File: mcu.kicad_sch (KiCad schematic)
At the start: 22 parts, among them J1 FTSH-105-01-F-DV-P-TR, U1 nRF52840, U5 MX25R6435FZAIL0, U6 AP22814AW5, Y1 32MHz, Y2 32.768kHz

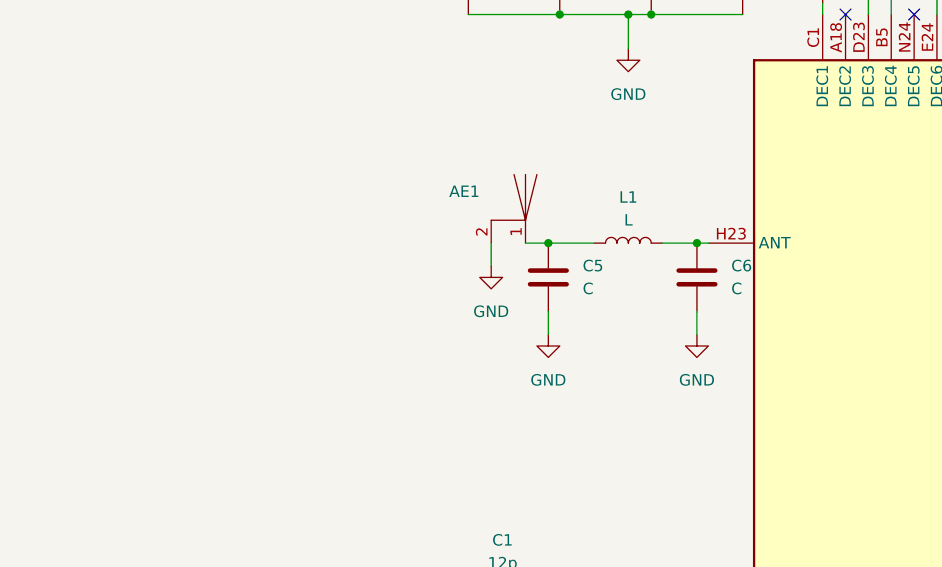
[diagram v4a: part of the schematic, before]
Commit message: Added impedance match, gitignore
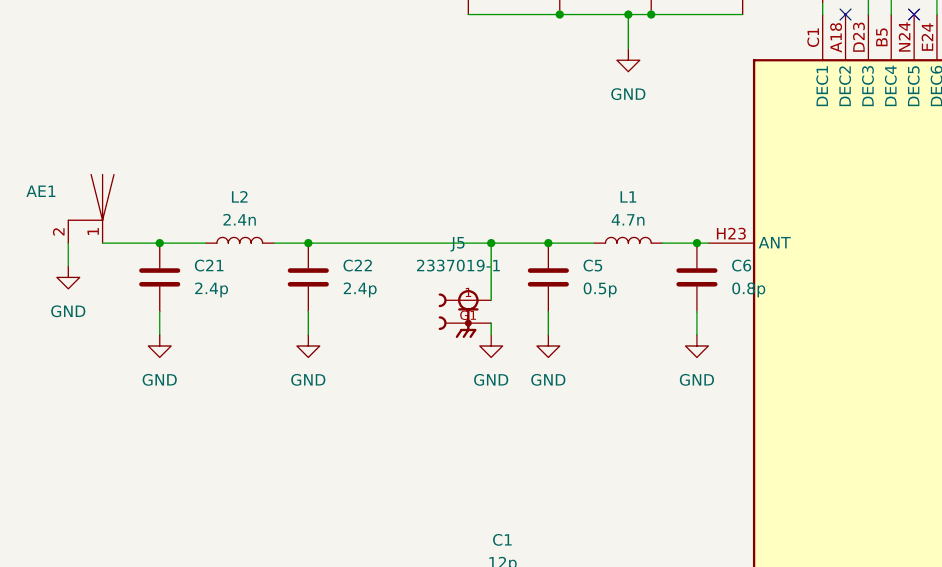
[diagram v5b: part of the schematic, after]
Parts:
- added C21, C22: 2.4p, symbol Device:C
- added J5: 2337019-1, Personal:TE_2337019-1, symbol generic:2337019-1
- added L2: 2.4n, symbol Device:L
- C5: value C -> 0.5p
- C6: value C -> 0.8p
- L1: value L -> 4.7n
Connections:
- net GND: now also C21.2, C22.2, J5.G1
- net at C5.1, L1.1: now also C22.1, J5.1, L2.2; no longer AE1.1
- new net: AE1.1, C21.1, L2.1
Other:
- moved on the sheet: AE1

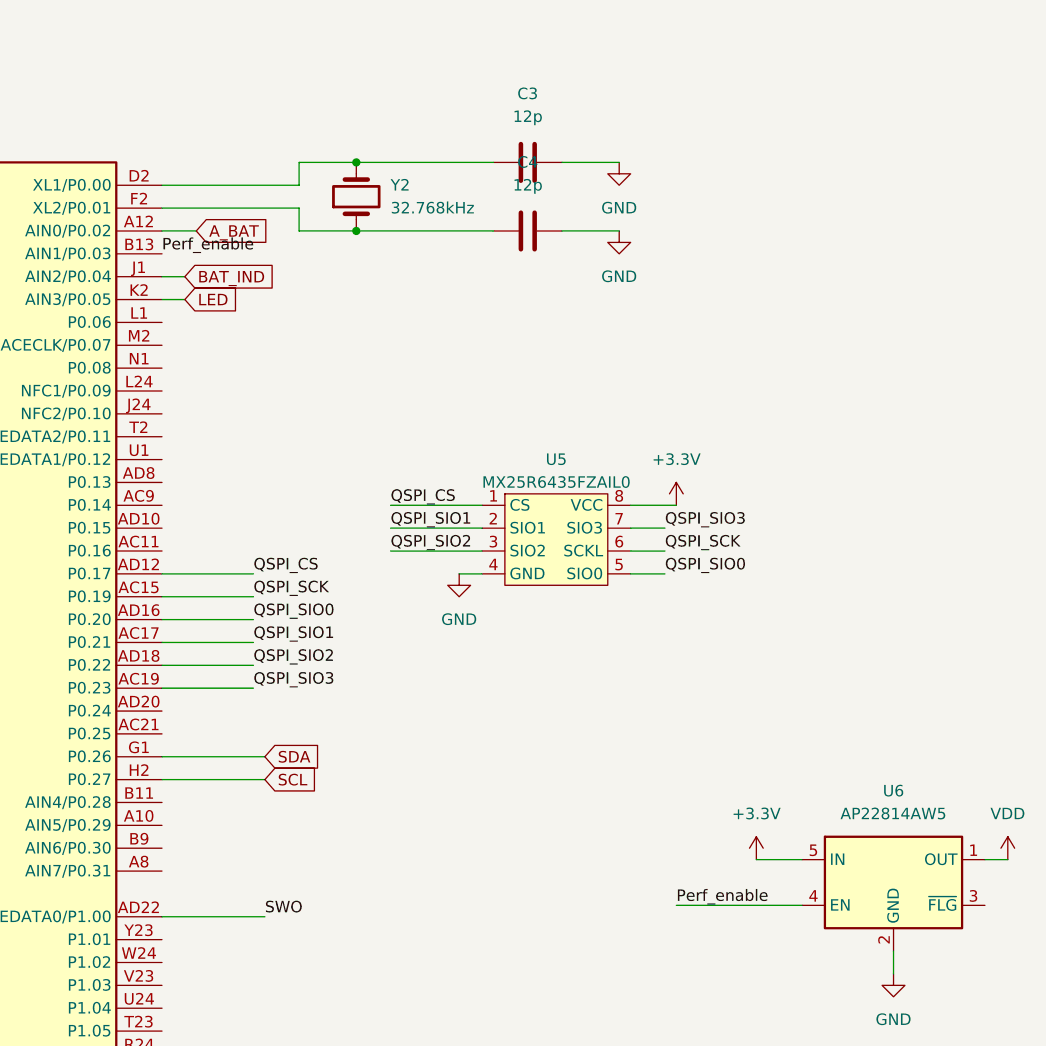
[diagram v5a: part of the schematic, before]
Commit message: Added microphone, fuse
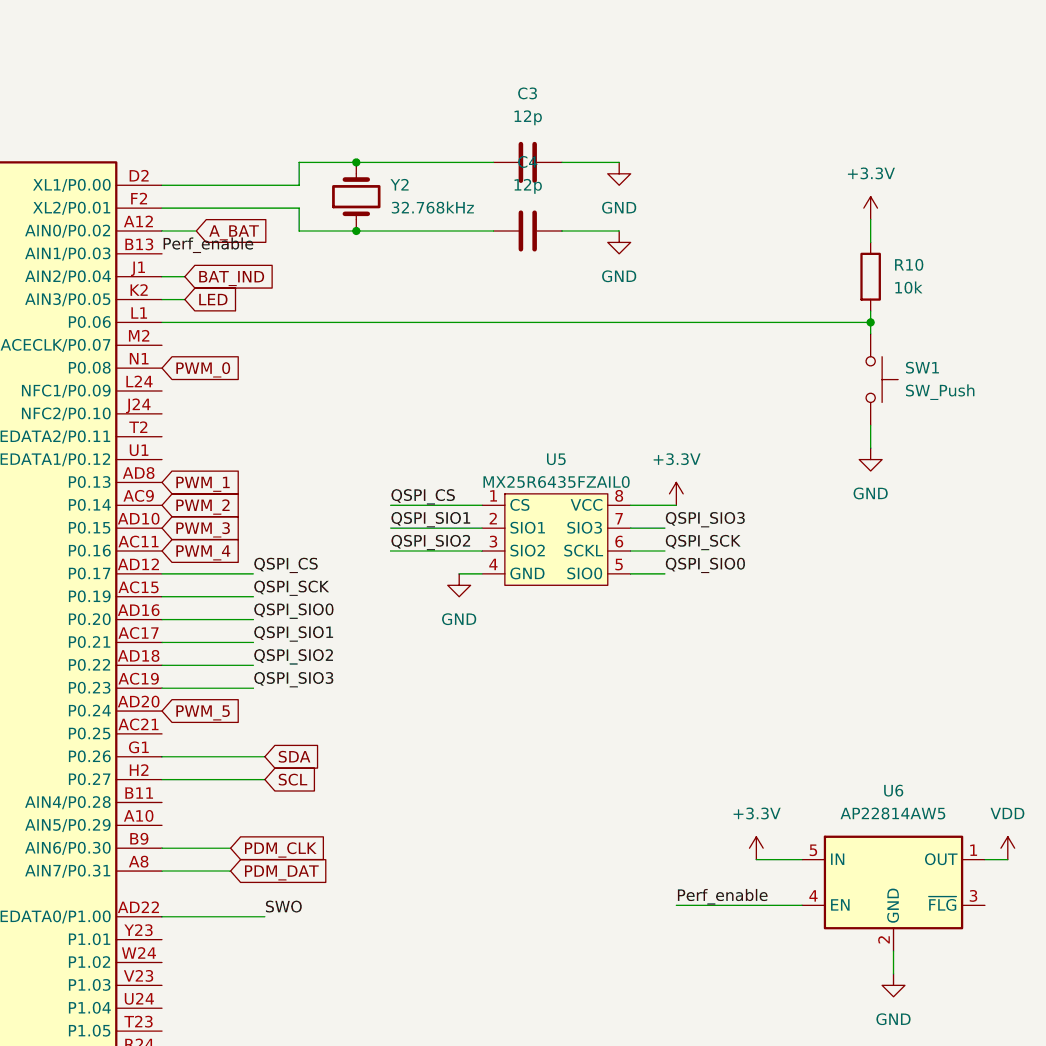
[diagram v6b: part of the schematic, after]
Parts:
- added R10: 10k, symbol Device:R
- added SW1: SW_Push, Button_Switch_THT:SW_PUSH_6mm, symbol Switch:SW_Push
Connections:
- net +3.3V: now also R10.1
- net GND: now also SW1.2
- net PDM_DAT: now reaches U1.A8 (AIN7/P0.31)
- net PWM_4: now reaches U1.AC11 (P0.16)
- net PWM_2: now reaches U1.AC9 (P0.14)
- net PWM_3: now reaches U1.AD10 (P0.15)
- net PWM_5: now reaches U1.AD20 (P0.24)
- net PWM_1: now reaches U1.AD8 (P0.13)
- net PDM_CLK: now reaches U1.B9 (AIN6/P0.30)
- net at U1.L1 (P0.06): now also R10.2, SW1.1
- net PWM_0: now reaches U1.N1 (P0.08)

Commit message: finished schematic
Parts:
- C1, C2, C3, C4: footprint (none) -> Capacitor_SMD:C_0603_1608Metric; LCSC PN (none) -> C107034
- C11, C17: footprint (none) -> Capacitor_SMD:C_0603_1608Metric; LCSC PN (none) -> C15849
- C12, C13, C16: value 100n -> .1u; footprint (none) -> Capacitor_SMD:C_0603_1608Metric; LCSC PN (none) -> C14663
- C14, C15: footprint (none) -> Capacitor_SMD:C_0603_1608Metric; LCSC PN (none) -> C19666
- C18: footprint (none) -> Capacitor_SMD:C_0603_1608Metric; LCSC PN (none) -> C14665
- C21, C22: footprint (none) -> Capacitor_SMD:C_0603_1608Metric; LCSC PN (none) -> C710896
- C5: footprint (none) -> Capacitor_SMD:C_0603_1608Metric; LCSC PN (none) -> C162254
- C6: footprint (none) -> Capacitor_SMD:C_0603_1608Metric; LCSC PN (none) -> C907996
- L1: footprint (none) -> Inductor_SMD:L_0603_1608Metric; LCSC PN (none) -> C98078
- L2: footprint (none) -> Inductor_SMD:L_0603_1608Metric; LCSC PN (none) -> C2042508
- R10: footprint (none) -> Resistor_SMD:R_0603_1608Metric; LCSC PN (none) -> C98220
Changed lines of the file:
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@@
 			)
 		)
-		(property "Footprint" ""
+		(property "Footprint" "Capacitor_SMD:C_0603_1608Metric"
 			(at 111.4552 20.32 0)
 			(effects
@@
 			)
 		)
+		(property "LCSC PN" "C14665"
+			(at 110.49 16.51 0)
+			(effects
+				(font
+					(size 1.27 1.27)
+				)
+				(hide yes)
+			)
+		)
 		(pin "2"
 		)
@@
 			)
 		)
-		(property "Footprint" ""
+		(property "Footprint" "Capacitor_SMD:C_0603_1608Metric"
 			(at 113.9952 25.4 0)
 			(effects
@@
 			)
 		)
+		(property "LCSC PN" "C15849"
+			(at 113.03 21.59 0)
+			(effects
+				(font
+					(size 1.27 1.27)
+				)
+				(hide yes)
+			)
+		)
 		(pin "2"
 		)
@@
 			)
 		)
-		(property "Value" "100n"
+		(property "Value" ".1u"
 			(at 100.33 25.3999 0)
 			(effects
@@
 			)
 		)
-		(property "Footprint" ""
+		(property "Footprint" "Capacitor_SMD:C_0603_1608Metric"
 			(at 97.4852 27.94 0)
 			(effects
@@
 			)
 		)
+		(property "LCSC PN" "C14663"
+			(at 96.52 24.13 0)
+			(effects
+				(font
+					(size 1.27 1.27)
+				)
+				(hide yes)
+			)
+		)
 		(pin "2"
 		)
@@
 			)
 		)
-		(property "Footprint" ""
+		(property "Footprint" "Capacitor_SMD:C_0603_1608Metric"
 			(at 72.39 103.1748 0)
 			(effects
@@
 			)
 		)
+		(property "LCSC PN" "C107034"
+			(at 68.58 104.14 90)
+			(effects
+				(font
+					(size 1.27 1.27)
+				)
+				(hide yes)
+			)
+		)
 		(pin "2"
 		)
@@
 			)
 		)
-		(property "Footprint" ""
+		(property "Footprint" "Capacitor_SMD:C_0603_1608Metric"
 			(at 75.8952 60.96 0)
 			(effects
@@
 			)
 		)
+		(property "LCSC PN" "C162254"
+			(at 74.93 57.15 0)
+			(effects
+				(font
+					(size 1.27 1.27)
+				)
+				(hide yes)
+			)
+		)
 		(pin "2"
 		)
@@
 			)
 		)
-		(property "Footprint" ""
+		(property "Footprint" "Inductor_SMD:L_0603_1608Metric"
 			(at 40.64 53.34 0)
 			(effects
@@
 			)
 		)
+		(property "LCSC PN" "C2042508"
+			(at 40.64 53.34 90)
+			(effects
+				(font
+					(size 1.27 1.27)
+				)
+				(hide yes)
+			)
+		)
 		(pin "2"
 		)
@@
 			)
 		)
-		(property "Value" "100n"
+		(property "Value" ".1u"
 			(at 109.22 24.1299 0)
 			(effects
@@
 			)
 		)
-		(property "Footprint" ""
+		(property "Footprint" "Capacitor_SMD:C_0603_1608Metric"
 			(at 106.3752 26.67 0)
 			(effects
@@
 			)
 		)
+		(property "LCSC PN" "C14663"
+			(at 105.41 22.86 0)
+			(effects
+				(font
+					(size 1.27 1.27)
+				)
+				(hide yes)
+			)
+		)
 		(pin "2"
 		)
@@
 			)
 		)
-		(property "Footprint" ""
+		(property "Footprint" "Capacitor_SMD:C_0603_1608Metric"
 			(at 32.7152 60.96 0)
 			(effects
@@
 			)
 		)
+		(property "LCSC PN" "C710896"
+			(at 31.75 57.15 0)
+			(effects
+				(font
+					(size 1.27 1.27)
+				)
+				(hide yes)
+			)
+		)
 		(pin "2"
 		)
@@
 			)
 		)
-		(property "Footprint" ""
+		(property "Footprint" "Capacitor_SMD:C_0603_1608Metric"
 			(at 77.1652 27.94 0)
 			(effects
@@
 			)
 		)
+		(property "LCSC PN" "C15849"
+			(at 76.2 24.13 0)
+			(effects
+				(font
+					(size 1.27 1.27)
+				)
+				(hide yes)
+			)
+		)
 		(pin "2"
 		)
@@
 			)
 		)
-		(property "Footprint" ""
+		(property "Footprint" "Inductor_SMD:L_0603_1608Metric"
 			(at 83.82 53.34 0)
 			(effects
@@
 			)
 		)
+		(property "LCSC PN" "C98078"
+			(at 83.82 53.34 90)
+			(effects
+				(font
+					(size 1.27 1.27)
+				)
+				(hide yes)
+			)
+		)
 		(pin "2"
 		)
@@
 			)
 		)
-		(property "Footprint" ""
+		(property "Footprint" "Capacitor_SMD:C_0603_1608Metric"
 			(at 119.6848 20.32 0)
 			(effects
@@
 			)
 		)
+		(property "LCSC PN" "C19666"
+			(at 120.65 24.13 0)
+			(effects
+				(font
+					(size 1.27 1.27)
+				)
+				(hide yes)
+			)
+		)
 		(pin "2"
 		)
@@
 			)
 		)
-		(property "Footprint" ""
+		(property "Footprint" "Capacitor_SMD:C_0603_1608Metric"
 			(at 203.2 32.0548 0)
 			(effects
@@
 			)
 		)
+		(property "LCSC PN" "C107034"
+			(at 199.39 33.02 90)
+			(effects
+				(font
+					(size 1.27 1.27)
+				)
+				(hide yes)
+			)
+		)
 		(pin "2"
 		)
@@
 			)
 		)
-		(property "Footprint" ""
+		(property "Footprint" "Capacitor_SMD:C_0603_1608Metric"
 			(at 92.4052 60.96 0)
 			(effects
@@
 			)
 		)
+		(property "LCSC PN" "C907996"
+			(at 91.44 57.15 0)
+			(effects
+				(font
+					(size 1.27 1.27)
+				)
+				(hide yes)
+			)
+		)
 		(pin "1"
 		)
@@
 			)
 		)
-		(property "Footprint" ""
+		(property "Footprint" "Resistor_SMD:R_0603_1608Metric"
 			(at 235.712 45.72 90)
 			(effects
@@
 			)
 		)
+		(property "LCSC PN" "C98220"
+			(at 237.49 45.72 0)
+			(effects
+				(font
+					(size 1.27 1.27)
+				)
+				(hide yes)
+			)
+		)
 		(pin "1"
 		)
@@
 			)
 		)
-		(property "Footprint" ""
+		(property "Footprint" "Capacitor_SMD:C_0603_1608Metric"
 			(at 203.2 39.6748 0)
 			(effects
@@
 			)
 		)
+		(property "LCSC PN" "C107034"
+			(at 199.39 40.64 90)
+			(effects
+				(font
+					(size 1.27 1.27)
+				)
+				(hide yes)
+			)
+		)
 		(pin "1"
 		)
@@
 			)
 		)
-		(property "Footprint" ""
+		(property "Footprint" "Capacitor_SMD:C_0603_1608Metric"
 			(at 67.0052 27.94 0)
 			(effects
@@
 			)
 		)
+		(property "LCSC PN" "C19666"
+			(at 66.04 24.13 0)
+			(effects
+				(font
+					(size 1.27 1.27)
+				)
+				(hide yes)
+			)
+		)
 		(pin "2"
 		)
@@
 			)
 		)
-		(property "Footprint" ""
+		(property "Footprint" "Capacitor_SMD:C_0603_1608Metric"
 			(at 73.66 93.0148 0)
 			(effects
@@
 			)
 		)
+		(property "LCSC PN" "C107034"
+			(at 69.85 93.98 90)
+			(effects
+				(font
+					(size 1.27 1.27)
+				)
+				(hide yes)
+			)
+		)
 		(pin "1"
 		)
@@
 			)
 		)
-		(property "Footprint" ""
+		(property "Footprint" "Capacitor_SMD:C_0603_1608Metric"
 			(at 49.2252 60.96 0)
 			(effects
@@
 			)
 		)
+		(property "LCSC PN" "C710896"
+			(at 48.26 57.15 0)
+			(effects
+				(font
+					(size 1.27 1.27)
+				)
+				(hide yes)
+			)
+		)
 		(pin "1"
 		)
@@
 			)
 		)
-		(property "Value" "100n"
+		(property "Value" ".1u"
 			(at 90.17 25.3999 0)
 			(effects
@@
 			)
 		)
-		(property "Footprint" ""
+		(property "Footprint" "Capacitor_SMD:C_0603_1608Metric"
 			(at 87.3252 27.94 0)
 			(effects
@@
 			(at 86.36 24.13 0)
 			(effects
+				(font
+					(size 1.27 1.27)
+				)
+				(hide yes)
+			)
+		)
+		(property "LCSC PN" "C14663"
+			(at 86.36 24.13 0)
+			(effects

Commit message: PCB layout
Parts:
- added C25: 1u, Capacitor_SMD:C_0603_1608Metric, symbol Device:C
- added R11, R12: 10k, Resistor_SMD:R_0603_1608Metric, symbol Device:R
- added R13: 100k, Resistor_SMD:R_0603_1608Metric, symbol Device:R
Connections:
- net +3.3V: now also R11.1, R12.1
- net GND: now also C25.2
- net SCL: now also R11.2
- net SDA: now also R12.2
- net at R10.2, SW1.1: now also R13.2; no longer U1.L1 (P0.06)
- net D+ renamed D_P
- net D- renamed D_N
- new net: C25.1, R13.1, U1.L1 (P0.06)
